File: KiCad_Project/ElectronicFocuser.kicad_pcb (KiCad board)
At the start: 2 copper layers, 38.9 x 43.2 mm, 4 parts, among them J1 JST-XH Stepper, U1 ULN2003

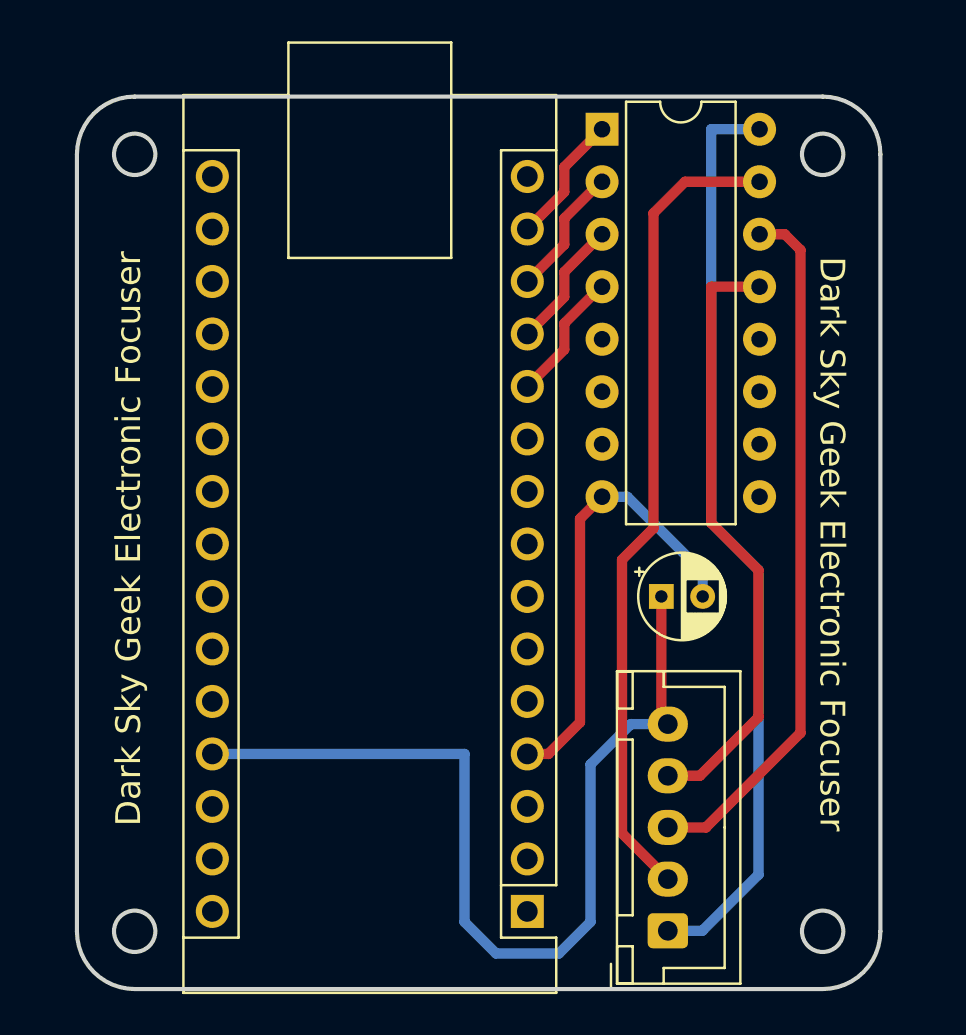
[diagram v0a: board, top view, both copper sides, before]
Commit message: Updated PCB layout to make room for attachments
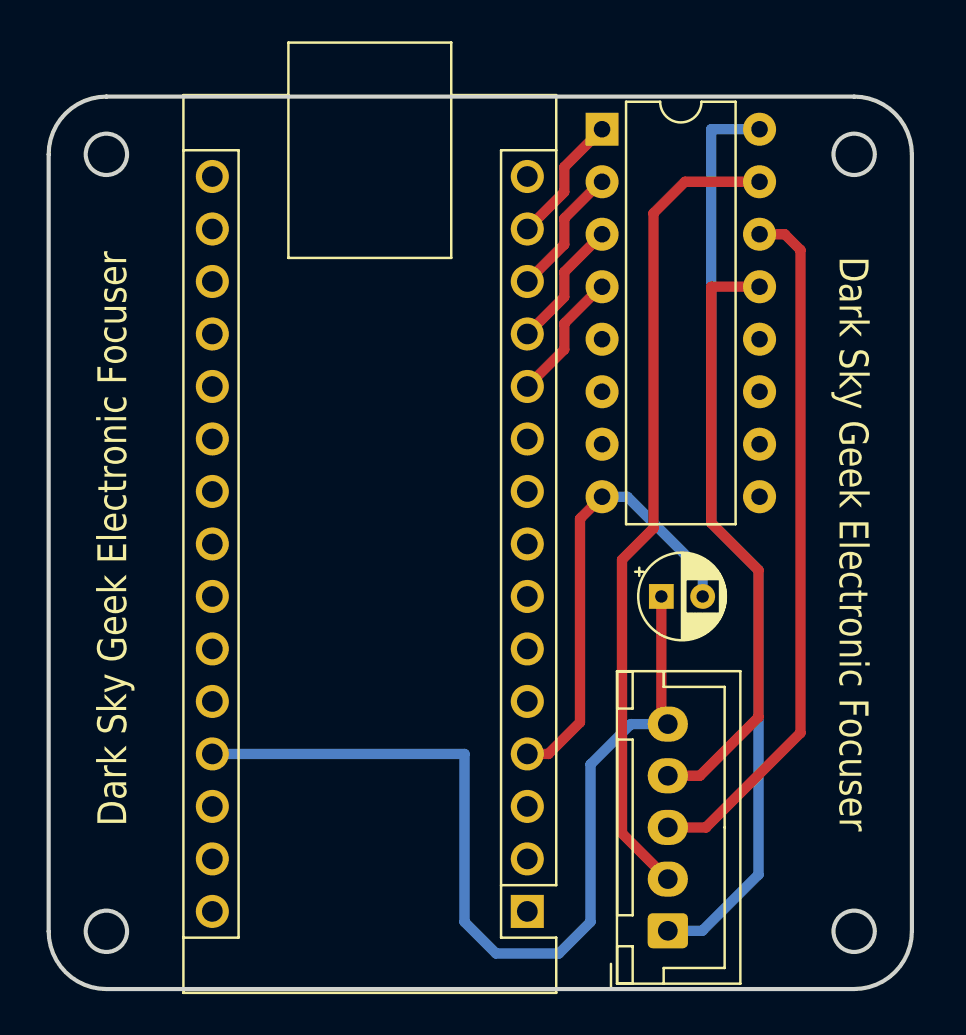
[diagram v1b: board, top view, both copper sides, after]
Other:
- board size 38.9 x 43.2 mm -> 41.8 x 43.2 mm
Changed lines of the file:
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@@
     )
   )
-  (gr_line (start 157.282366 76.905634) (end 157.282366 114.5) (layer "Edge.Cuts") (width 0.2))
-  (gr_arc (start 121.2 117.294) (mid 119.224344 116.475656) (end 118.406 114.5) (layer "Edge.Cuts") (width 0.2))
-  (gr_line (start 118.406 76.905656) (end 118.406 114.5) (layer "Edge.Cuts") (width 0.2))
-  (gr_circle (center 121.2 114.5) (end 122.2 114.5) (layer "Edge.Cuts") (width 0.2) (fill none))
-  (gr_arc (start 154.488366 74.111634) (mid 156.464 74.93) (end 157.282366 76.905634) (layer "Edge.Cuts") (width 0.2))
-  (gr_arc (start 157.282366 114.5) (mid 156.464022 116.475656) (end 154.488366 117.294) (layer "Edge.Cuts") (width 0.2))
-  (gr_arc (start 118.406 76.905656) (mid 119.224359 74.930028) (end 121.2 74.111656) (layer "Edge.Cuts") (width 0.2))
-  (gr_circle (center 154.488366 114.5) (end 155.488366 114.5) (layer "Edge.Cuts") (width 0.2) (fill none))
-  (gr_circle (center 121.2 76.905656) (end 122.2 76.905656) (layer "Edge.Cuts") (width 0.2) (fill none))
-  (gr_line (start 154.488366 117.294) (end 121.2 117.294022) (layer "Edge.Cuts") (width 0.2))
-  (gr_line (start 121.2 74.111656) (end 154.488366 74.111634) (layer "Edge.Cuts") (width 0.2))
-  (gr_circle (center 154.488366 76.905656) (end 155.488366 76.905656) (layer "Edge.Cuts") (width 0.2) (fill none))
-  (gr_text "Dark Sky Geek Electronic Focuser" (at 120.904 95.504 90) (layer "F.SilkS")
-    (effects (font (size 1.2 1.2) (thickness 0.2)))
+  (gr_line (start 158.806363 76.905634) (end 158.806346 114.5) (layer "Edge.Cuts") (width 0.2))
+  (gr_arc (start 119.831656 117.294) (mid 117.856 116.475656) (end 117.037656 114.5) (layer "Edge.Cuts") (width 0.2))
+  (gr_line (start 117.037647 76.905656) (end 117.037656 114.5) (layer "Edge.Cuts") (width 0.2))
+  (gr_circle (center 119.831656 114.5) (end 120.831656 114.5) (layer "Edge.Cuts") (width 0.2) (fill none))
+  (gr_arc (start 156.012363 74.111634) (mid 157.988 74.929997) (end 158.806363 76.905634) (layer "Edge.Cuts") (width 0.2))
+  (gr_arc (start 158.806346 114.5) (mid 157.988 116.475644) (end 156.012346 117.294) (layer "Edge.Cuts") (width 0.2))
+  (gr_arc (start 117.037647 76.905656) (mid 117.856 74.929993) (end 119.831647 74.111656) (layer "Edge.Cuts") (width 0.2))
+  (gr_circle (center 156.01238 114.5) (end 157.01238 114.5) (layer "Edge.Cuts") (width 0.2) (fill none))
+  (gr_circle (center 119.831747 76.9057) (end 120.831747 76.9057) (layer "Edge.Cuts") (width 0.2) (fill none))
+  (gr_line (start 156.012346 117.294) (end 119.831656 117.294) (layer "Edge.Cuts") (width 0.2))
+  (gr_line (start 119.831647 74.111656) (end 156.012363 74.111634) (layer "Edge.Cuts") (width 0.2))
+  (gr_circle (center 156.012297 76.9057) (end 157.012297 76.9057) (layer "Edge.Cuts") (width 0.2) (fill none))
+  (gr_text "Dark Sky Geek Electronic Focuser" (at 120.142 95.504 90) (layer "F.SilkS")
+    (effects (font (size 1.4 1.2) (thickness 0.2)))
   )
-  (gr_text "Dark Sky Geek Electronic Focuser" (at 154.94 95.758 -90) (layer "F.SilkS")
-    (effects (font (size 1.2 1.2) (thickness 0.2)))
+  (gr_text "Dark Sky Geek Electronic Focuser" (at 155.956 95.758 -90) (layer "F.SilkS")
+    (effects (font (size 1.4 1.2) (thickness 0.2)))
   )
   (segment (start 143.8154 83.312) (end 143.764 83.312) (width 0.5) (layer "F.Cu") (net 11))

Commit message: Updated PCB layout to make room for attachments
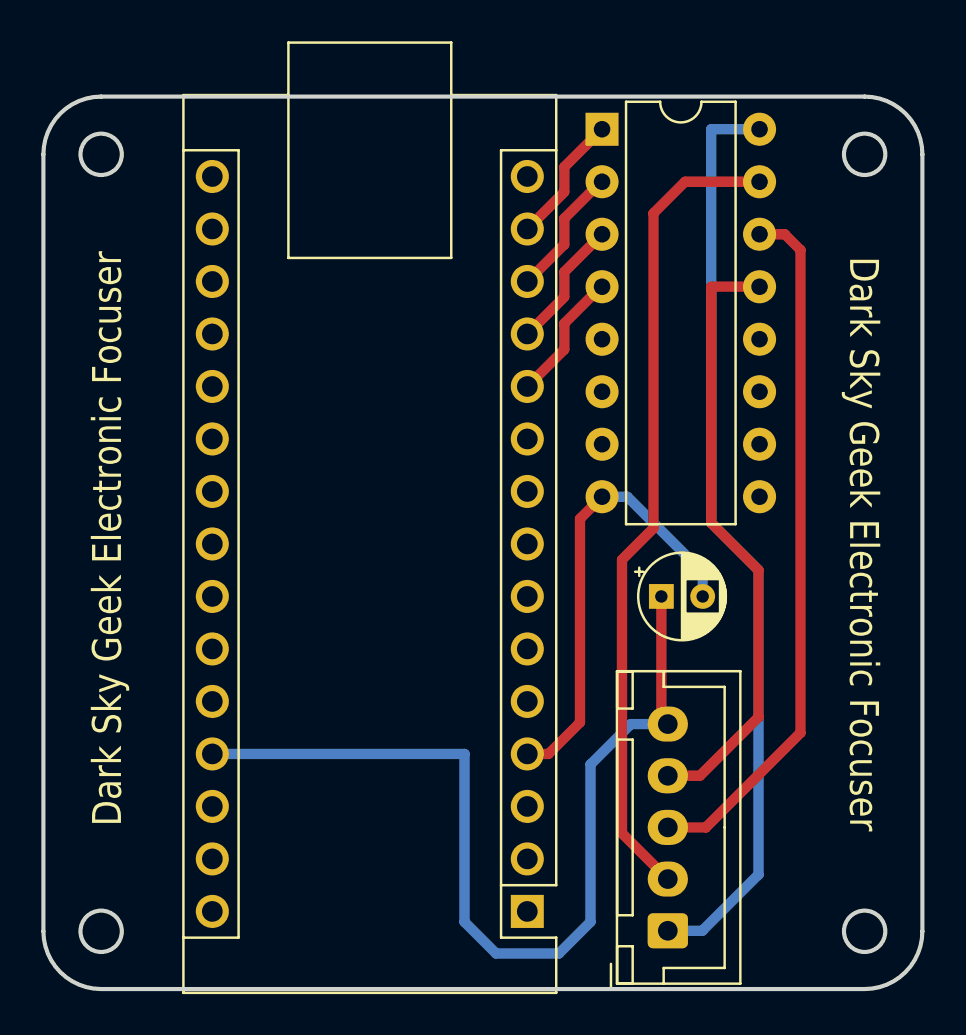
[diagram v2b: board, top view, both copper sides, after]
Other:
- board size 41.8 x 43.2 mm -> 42.5 x 43.2 mm
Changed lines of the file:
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@@
     )
   )
-  (gr_line (start 158.806363 76.905634) (end 158.806346 114.5) (layer "Edge.Cuts") (width 0.2))
-  (gr_arc (start 119.831656 117.294) (mid 117.856 116.475656) (end 117.037656 114.5) (layer "Edge.Cuts") (width 0.2))
-  (gr_line (start 117.037647 76.905656) (end 117.037656 114.5) (layer "Edge.Cuts") (width 0.2))
-  (gr_circle (center 119.831656 114.5) (end 120.831656 114.5) (layer "Edge.Cuts") (width 0.2) (fill none))
-  (gr_arc (start 156.012363 74.111634) (mid 157.988 74.929997) (end 158.806363 76.905634) (layer "Edge.Cuts") (width 0.2))
-  (gr_arc (start 158.806346 114.5) (mid 157.988 116.475644) (end 156.012346 117.294) (layer "Edge.Cuts") (width 0.2))
-  (gr_arc (start 117.037647 76.905656) (mid 117.856 74.929993) (end 119.831647 74.111656) (layer "Edge.Cuts") (width 0.2))
-  (gr_circle (center 156.01238 114.5) (end 157.01238 114.5) (layer "Edge.Cuts") (width 0.2) (fill none))
-  (gr_circle (center 119.831747 76.9057) (end 120.831747 76.9057) (layer "Edge.Cuts") (width 0.2) (fill none))
-  (gr_line (start 156.012346 117.294) (end 119.831656 117.294) (layer "Edge.Cuts") (width 0.2))
-  (gr_line (start 119.831647 74.111656) (end 156.012363 74.111634) (layer "Edge.Cuts") (width 0.2))
-  (gr_circle (center 156.012297 76.9057) (end 157.012297 76.9057) (layer "Edge.Cuts") (width 0.2) (fill none))
-  (gr_text "Dark Sky Geek Electronic Focuser" (at 120.142 95.504 90) (layer "F.SilkS")
+  (gr_line (start 159.314363 76.905634) (end 159.314346 114.5) (layer "Edge.Cuts") (width 0.2))
+  (gr_arc (start 119.577656 117.294) (mid 117.602 116.475656) (end 116.783656 114.5) (layer "Edge.Cuts") (width 0.2))
+  (gr_line (start 116.783647 76.905656) (end 116.783656 114.5) (layer "Edge.Cuts") (width 0.2))
+  (gr_circle (center 119.577656 114.5) (end 120.577656 114.5) (layer "Edge.Cuts") (width 0.2) (fill none))
+  (gr_arc (start 156.520363 74.111634) (mid 158.496 74.929997) (end 159.314363 76.905634) (layer "Edge.Cuts") (width 0.2))
+  (gr_arc (start 159.314346 114.5) (mid 158.496 116.475644) (end 156.520346 117.294) (layer "Edge.Cuts") (width 0.2))
+  (gr_arc (start 116.783647 76.905656) (mid 117.602 74.929993) (end 119.577647 74.111656) (layer "Edge.Cuts") (width 0.2))
+  (gr_circle (center 156.52038 114.5) (end 157.52038 114.5) (layer "Edge.Cuts") (width 0.2) (fill none))
+  (gr_circle (center 119.577747 76.9057) (end 120.577747 76.9057) (layer "Edge.Cuts") (width 0.2) (fill none))
+  (gr_line (start 156.520346 117.294) (end 119.577656 117.294) (layer "Edge.Cuts") (width 0.2))
+  (gr_line (start 119.577647 74.111656) (end 156.520363 74.111634) (layer "Edge.Cuts") (width 0.2))
+  (gr_circle (center 156.520297 76.9057) (end 157.520297 76.9057) (layer "Edge.Cuts") (width 0.2) (fill none))
+  (gr_text "Dark Sky Geek Electronic Focuser" (at 119.888 95.504 90) (layer "F.SilkS")
     (effects (font (size 1.4 1.2) (thickness 0.2)))
   )
-  (gr_text "Dark Sky Geek Electronic Focuser" (at 155.956 95.758 -90) (layer "F.SilkS")
+  (gr_text "Dark Sky Geek Electronic Focuser" (at 156.464 95.758 -90) (layer "F.SilkS")
     (effects (font (size 1.4 1.2) (thickness 0.2)))
   )

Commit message: Forgot to connect pin 9 of ULN2003, which could cause electrical issues due to EMF
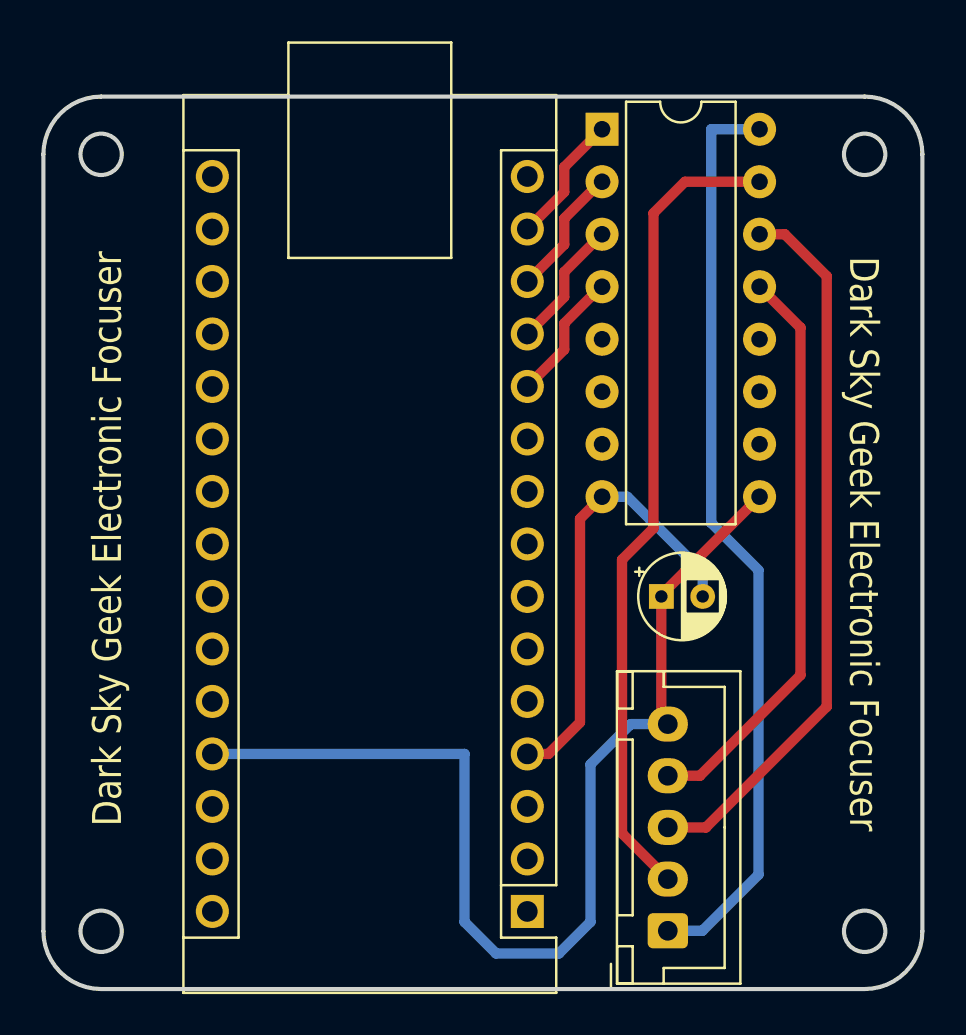
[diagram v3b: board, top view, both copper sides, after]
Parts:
- C1: value 10µF -> 10 µF
- J1: value JST-XH Stepper -> JST-XH Stepper Motor
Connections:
- U1 pad 9: unconnected-(U1-Pad9) -> Net-(A1-Pad27)
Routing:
- net Net-(A1-Pad27): track 46.2 -> 53.0 mm
- net Net-(J1-Pad4): track 29.7 -> 28.1 mm
- net Net-(J1-Pad3): track 34.0 -> 35.0 mm
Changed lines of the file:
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@@
   (net 36 "unconnected-(U1-Pad6)")
   (net 37 "unconnected-(U1-Pad7)")
-  (net 38 "unconnected-(U1-Pad9)")
-  (net 39 "unconnected-(U1-Pad10)")
-  (net 40 "unconnected-(U1-Pad11)")
-  (net 41 "unconnected-(U1-Pad12)")
+  (net 38 "unconnected-(U1-Pad10)")
+  (net 39 "unconnected-(U1-Pad11)")
+  (net 40 "unconnected-(U1-Pad12)")
   (footprint "Module:Arduino_Nano" (layer "F.Cu")
     (at 140.198 113.538 180)
@@
       (net 29 "GND") (pinfunction "GND") (pintype "power_in"))
     (pad "9" thru_hole oval (at 7.62 17.78) (size 1.6 1.6) (drill 0.8) (layers *.Cu *.Mask)
-      (net 38 "unconnected-(U1-Pad9)") (pinfunction "COM") (pintype "passive"))
+      (net 27 "Net-(A1-Pad27)") (pinfunction "COM") (pintype "passive"))
     (pad "10" thru_hole oval (at 7.62 15.24) (size 1.6 1.6) (drill 0.8) (layers *.Cu *.Mask)
-      (net 39 "unconnected-(U1-Pad10)") (pinfunction "O7") (pintype "open_collector"))
+      (net 38 "unconnected-(U1-Pad10)") (pinfunction "O7") (pintype "open_collector"))
     (pad "11" thru_hole oval (at 7.62 12.7) (size 1.6 1.6) (drill 0.8) (layers *.Cu *.Mask)
-      (net 40 "unconnected-(U1-Pad11)") (pinfunction "O6") (pintype "open_collector"))
+      (net 39 "unconnected-(U1-Pad11)") (pinfunction "O6") (pintype "open_collector"))
     (pad "12" thru_hole oval (at 7.62 10.16) (size 1.6 1.6) (drill 0.8) (layers *.Cu *.Mask)
-      (net 41 "unconnected-(U1-Pad12)") (pinfunction "O5") (pintype "open_collector"))
+      (net 40 "unconnected-(U1-Pad12)") (pinfunction "O5") (pintype "open_collector"))
     (pad "13" thru_hole oval (at 7.62 7.62) (size 1.6 1.6) (drill 0.8) (layers *.Cu *.Mask)
       (net 34 "Net-(J1-Pad4)") (pinfunction "O4") (pintype "open_collector"))
@@
       (effects (font (size 1 1) (thickness 0.15)))
     )
-    (fp_text value "JST-XH Stepper" (at 4.746 5.149599 90) (layer "F.SilkS") hide
+    (fp_text value "JST-XH Stepper Motor" (at 4.746 5.149599 90) (layer "F.SilkS") hide
       (effects (font (size 1 1) (thickness 0.15)))
     )
@@
       (effects (font (size 1 1) (thickness 0.15)))
     )
-    (fp_text value "10µF" (at 5.716396 0) (layer "F.SilkS") hide
+    (fp_text value "10 µF" (at 5.716396 0) (layer "F.SilkS") hide
       (effects (font (size 1 1) (thickness 0.15)))
     )
@@
   (segment (start 143.8154 75.692) (end 141.986 77.5214) (width 0.5) (layer "F.Cu") (net 14))
   (segment (start 146.6836 104.1612) (end 146.9964 104.474) (width 0.5) (layer "F.Cu") (net 27))
+  (segment (start 146.6836 98.298) (end 146.6836 98.2238) (width 0.5) (layer "F.Cu") (net 27))
+  (segment (start 146.6836 98.2238) (end 151.4354 93.472) (width 0.5) (layer "F.Cu") (net 27))
   (segment (start 146.6836 98.298) (end 146.6836 104.1612) (width 0.5) (layer "F.Cu") (net 27))
   (segment (start 141.732 115.57) (end 138.684 115.57) (width 0.5) (layer "B.Cu") (net 27))
@@
   (segment (start 144.78 109.7576) (end 144.78 96.52) (width 0.5) (layer "F.Cu") (net 32))
   (segment (start 144.78 96.52) (end 146.304 94.996) (width 0.5) (layer "F.Cu") (net 32))
-  (segment (start 148.844 109.474) (end 153.416 104.902) (width 0.5) (layer "F.Cu") (net 33))
+  (segment (start 146.9964 109.474) (end 148.844 109.474) (width 0.5) (layer "F.Cu") (net 33))
+  (segment (start 148.844 109.474) (end 154.686 103.632) (width 0.5) (layer "F.Cu") (net 33))
+  (segment (start 154.686 82.804) (end 152.654 80.772) (width 0.5) (layer "F.Cu") (net 33))
   (segment (start 152.654 80.772) (end 151.4354 80.772) (width 0.5) (layer "F.Cu") (net 33))
-  (segment (start 146.9964 109.474) (end 148.844 109.474) (width 0.5) (layer "F.Cu") (net 33))
-  (segment (start 153.416 104.902) (end 153.416 81.534) (width 0.5) (layer "F.Cu") (net 33))
-  (segment (start 153.416 81.534) (end 152.654 80.772) (width 0.5) (layer "F.Cu") (net 33))
-  (segment (start 149.098 83.312) (end 151.4354 83.312) (width 0.5) (layer "F.Cu") (net 34))
-  (segment (start 151.384 104.14) (end 151.384 97.028) (width 0.5) (layer "F.Cu") (net 34))
+  (segment (start 154.686 103.632) (end 154.686 82.804) (width 0.5) (layer "F.Cu") (net 33))
   (segment (start 146.9964 106.974) (end 148.55 106.974) (width 0.5) (layer "F.Cu") (net 34))
-  (segment (start 149.098 94.742) (end 149.098 83.312) (width 0.5) (layer "F.Cu") (net 34))
-  (segment (start 151.384 97.028) (end 149.098 94.742) (width 0.5) (layer "F.Cu") (net 34))
-  (segment (start 148.55 106.974) (end 151.384 104.14) (width 0.5) (layer "F.Cu") (net 34))
+  (segment (start 153.416 102.108) (end 153.416 85.2926) (width 0.5) (layer "F.Cu") (net 34))
+  (segment (start 153.416 85.2926) (end 151.4354 83.312) (width 0.5) (layer "F.Cu") (net 34))
+  (segment (start 148.55 106.974) (end 153.416 102.108) (width 0.5) (layer "F.Cu") (net 34))
 )
